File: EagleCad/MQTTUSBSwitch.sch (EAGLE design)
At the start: 41 parts, among them J1 10117835-002LF, J2 GSB4211311WEU, Q1 MMBT2222, Q2 MMBT2222, Q3 MMBT2222, Q4 MMBT2222, U1 MIC5504-3.3YM5_TR, X2 MICROBUILDER_RELAY_LATCHINGEE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, X3 MICROBUILDER_RELAY_LATCHINGEE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

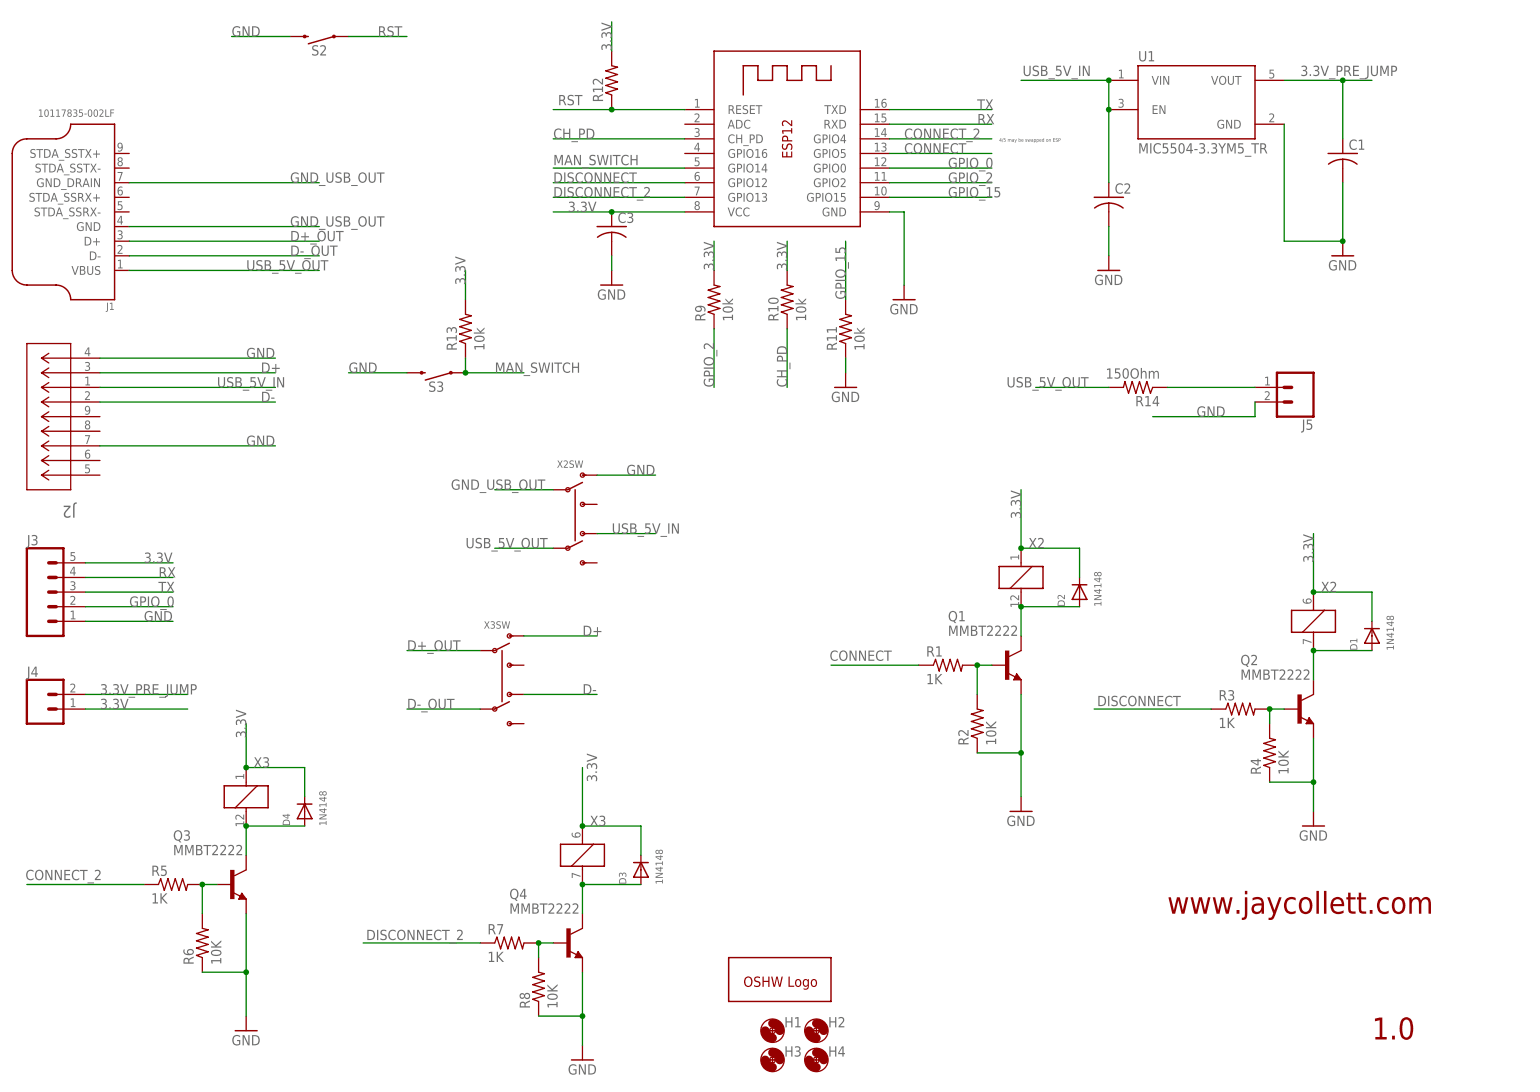
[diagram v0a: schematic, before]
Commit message: first pass at v2.1 which simplifies relay driving with a unla2803 and a port expander to only use 2 GPIO pins on ESP8266
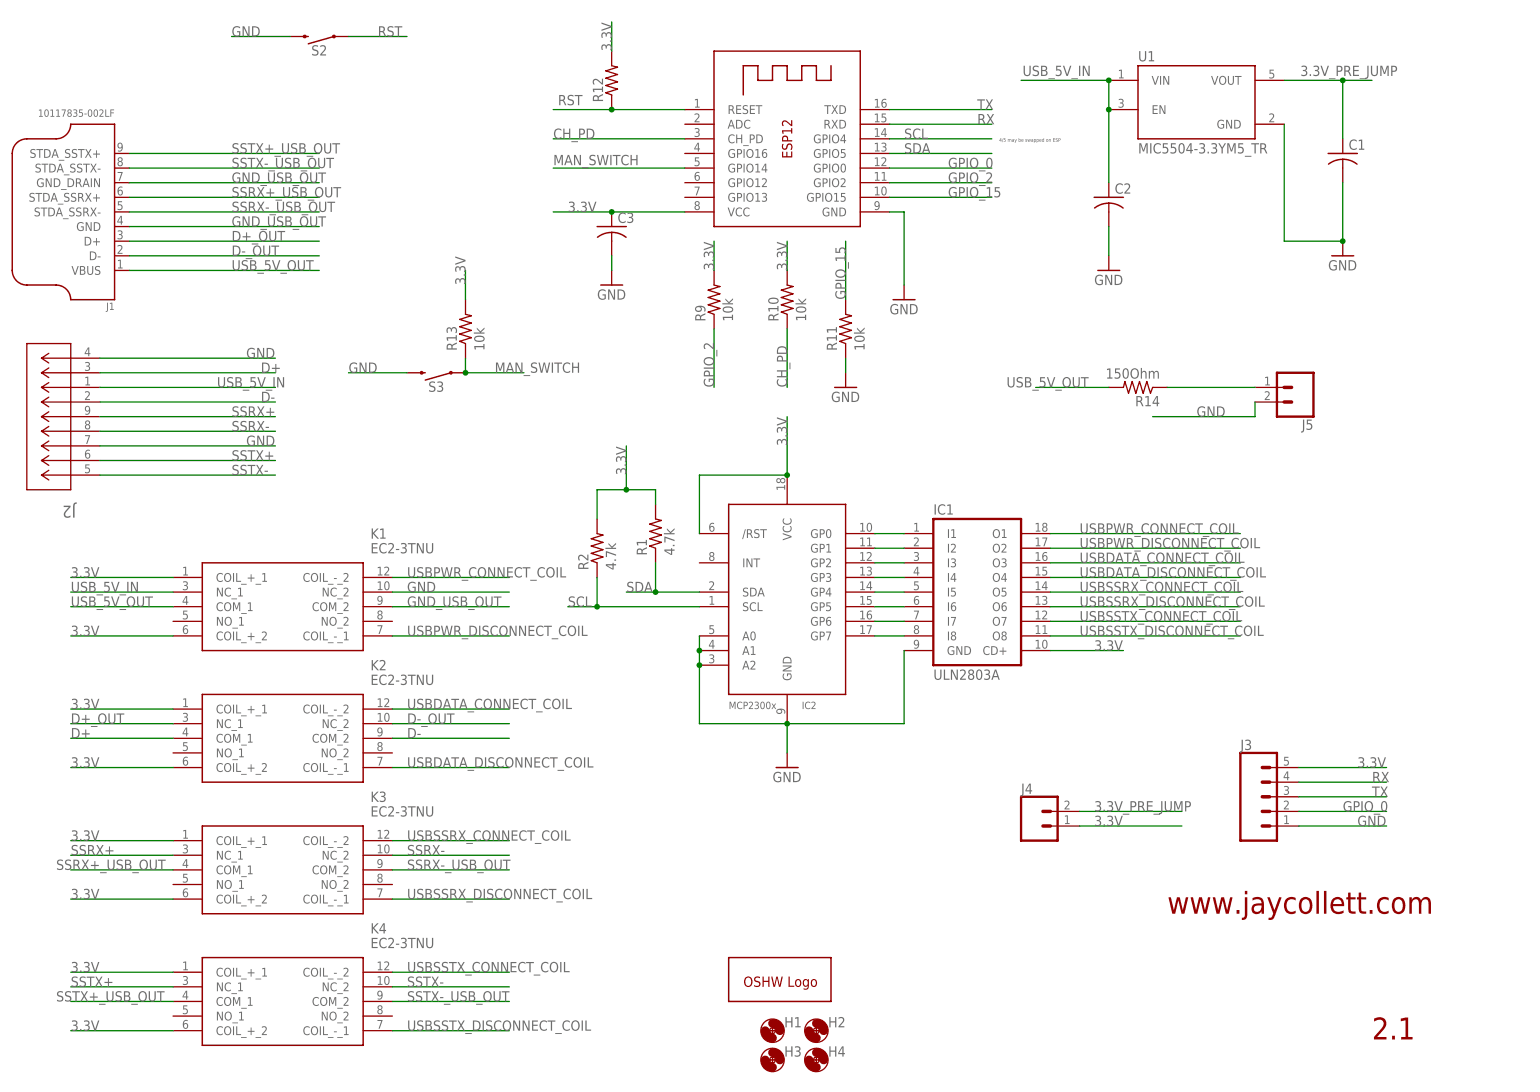
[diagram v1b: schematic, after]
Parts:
- removed D1, D2, D3, D4: 1N4148, adafruit:DIODESOD-323F
- removed Q1, Q2, Q3, Q4: MMBT2222, MMBT2222_:MMBT2222
- removed R3, R5, R7: 1K, adafruit:R-US_M0805
- removed R4, R6, R8: 10K, adafruit:R-US_M0805
- removed X2, X3: MICROBUILDER_RELAY_LATCHINGEE2NUH, AdaFruitLatchingRelay:MICROBUILDER_RELAY_LATCHINGEE2NUH
- added IC1: ULN2803A, uln-udn:ULN2804A
- added IC2: MCP23008/P, adafruit:MCP23008/P
- added K1, K2, K3, K4: EC2-3TNU, SamacSys_Parts:EC2-3TNU
- R1: value 1K -> 4.7k; device adafruit:R-US_M0805 -> adafruit:R-US_R0805
- R2: value 10K -> 4.7k; device adafruit:R-US_M0805 -> adafruit:R-US_R0805
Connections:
- removed net CONNECT: R1.1, X1.GPIO5
- removed net CONNECT_2: R5.1, X1.GPIO4
- removed net DISCONNECT: R3.1, X1.GPIO12
- removed net DISCONNECT_2: R7.1, X1.GPIO13
- removed net N$10: D2.A, Q1.C, X2SET.2
- removed net N$11: D1.A, Q2.C, X2RESET.2
- removed net N$12: Q1.B, R1.2, R2.2
- removed net N$13: Q2.B, R3.2, R4.2
- removed net N$14: D4.A, Q3.C, X3SET.2
- removed net N$15: D3.A, Q4.C, X3RESET.2
- removed net N$16: Q3.B, R5.2, R6.2
- removed net N$17: Q4.B, R7.2, R8.2
- new net N$2: IC1.I1, IC2.GP0
- new net N$3: IC1.I2, IC2.GP1
- new net N$4: IC1.I3, IC2.GP2
- new net N$5: IC1.I4, IC2.GP3
- new net N$6: IC1.I5, IC2.GP4
- new net N$7: IC1.I6, IC2.GP5
- new net N$8: IC1.I7, IC2.GP6
- new net N$9: IC1.I8, IC2.GP7
- new net SCL: IC2.SCL, R2.1, X1.GPIO4
- new net SDA: IC2.SDA, R1.1, X1.GPIO5
- new net SSRX+: J2.9, K3.NC_1
- new net SSRX+_USB_OUT: J1.STDA_SSRX+, K3.COM_1
- new net SSRX-: J2.8, K3.NC_2
- new net SSRX-_USB_OUT: J1.STDA_SSRX-, K3.COM_2
- new net SSTX+: J2.6, K4.NC_1
- new net SSTX+_USB_OUT: J1.STDA_SSTX+, K4.COM_1
- new net SSTX-: J2.5, K4.NC_2
- new net SSTX-_USB_OUT: J1.STDA_SSTX-, K4.COM_2
- new net USBDATA_CONNECT_COIL: IC1.O3, K2.COIL_-_2
- new net USBDATA_DISCONNECT_COIL: IC1.O4, K2.COIL_-_1
- new net USBPWR_CONNECT_COIL: IC1.O1, K1.COIL_-_2
- new net USBPWR_DISCONNECT_COIL: IC1.O2, K1.COIL_-_1
- new net USBSSRX_CONNECT_COIL: IC1.O5, K3.COIL_-_2
- new net USBSSRX_DISCONNECT_COIL: IC1.O6, K3.COIL_-_1
- new net USBSSTX_CONNECT_COIL: IC1.O7, K4.COIL_-_2
- new net USBSSTX_DISCONNECT_COIL: IC1.O8, K4.COIL_-_1
- net 3.3V: now also IC1.CD+, IC2./RST, IC2.VCC, K1.COIL_+_1, K1.COIL_+_2, K2.COIL_+_1, K2.COIL_+_2, K3.COIL_+_1, K3.COIL_+_2, K4.COIL_+_1, K4.COIL_+_2, R1.2, R2.2; no longer D1.C, D2.C, D3.C, D4.C, X2RESET.1, X2SET.1, X3RESET.1, X3SET.1
- net D+: now also K2.COM_1; no longer X3SW.O1
- net D+_OUT: now also K2.NC_1; no longer X3SW.P1
- net D-: now also K2.COM_2; no longer X3SW.O2
- net D-_OUT: now also K2.NC_2; no longer X3SW.P2
- net GND: now also IC1.GND, IC2.A0, IC2.A1, IC2.A2, IC2.GND, K1.NC_2; no longer Q1.E, Q2.E, Q3.E, Q4.E, R2.1, R4.1, R6.1, R8.1, X2SW.O1
- net GND_USB_OUT: now also K1.COM_2; no longer X2SW.P1
- net USB_5V_IN: now also K1.NC_1; no longer X2SW.O2
- net USB_5V_OUT: now also K1.COM_1; no longer X2SW.P2
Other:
- note added: "2.1"
- note removed: "1.0"
- moved on the sheet: J3, J4, R1, R2

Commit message: New layout and routing for v2.1
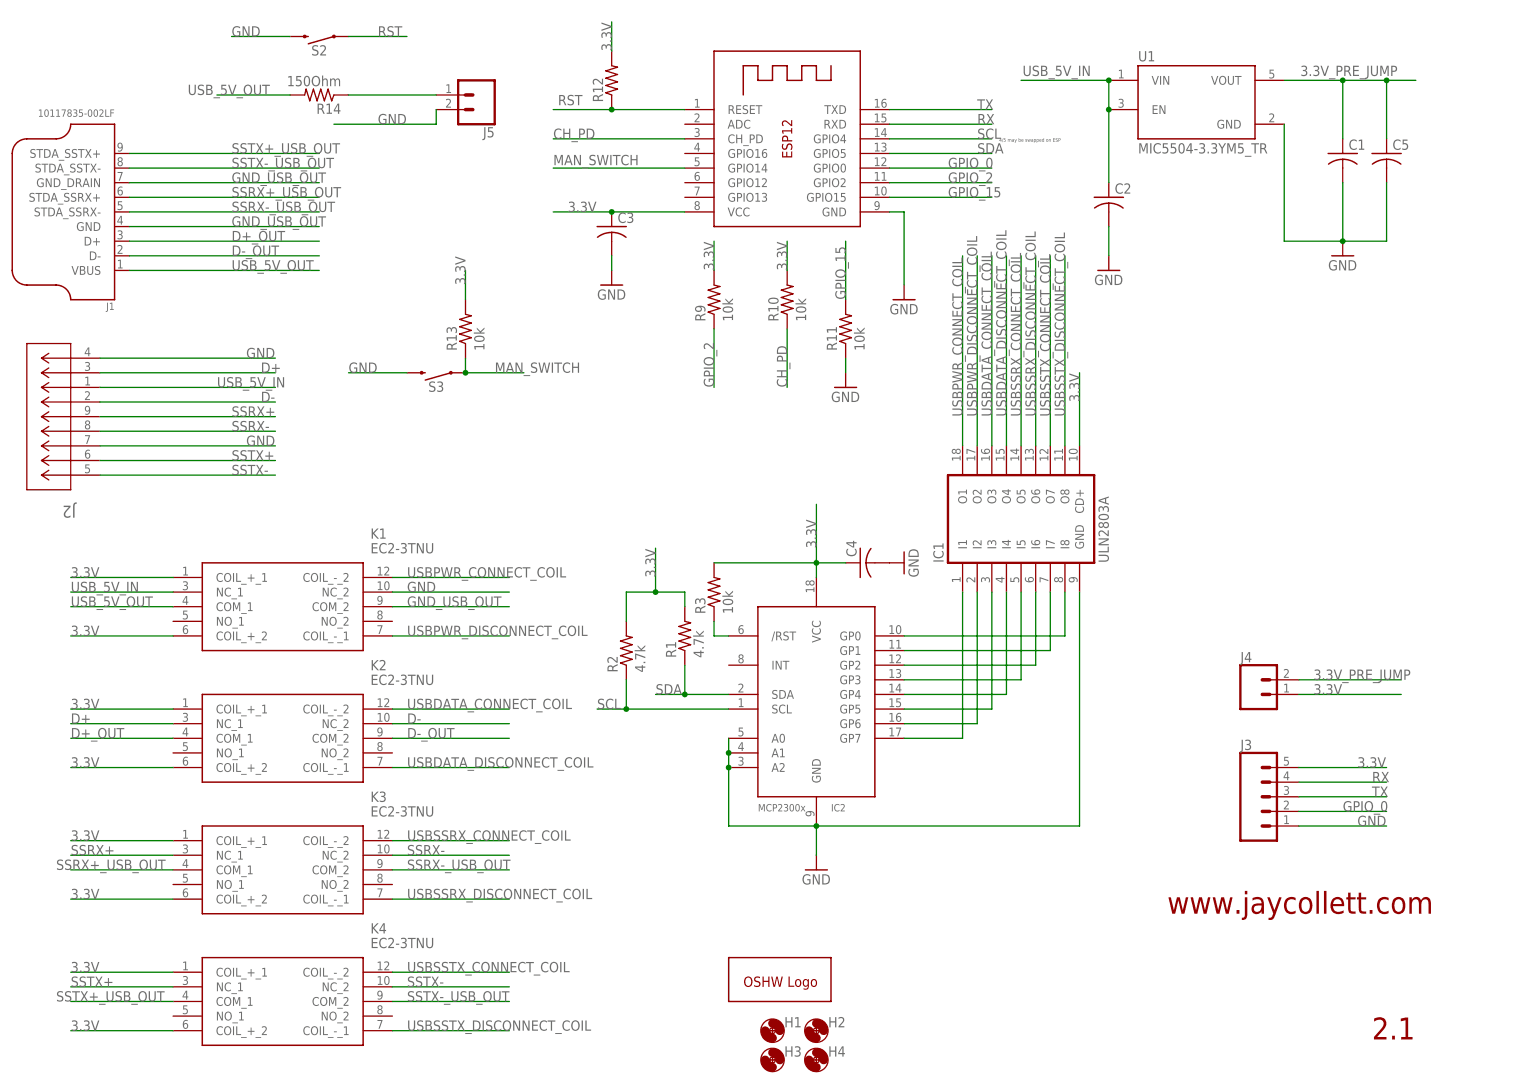
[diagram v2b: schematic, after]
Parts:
- added C4, C5: (no value), adafruit:C-USC0805
- added R3: 10k, adafruit:R-US_R0805
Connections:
- new net N$10: IC2./RST, R3.1
- net 3.3V: now also C4.1, R3.2; no longer IC2./RST
- net 3.3V_PRE_JUMP: now also C5.1
- net D+: now also K2.NC_1; no longer K2.COM_1
- net D+_OUT: now also K2.COM_1; no longer K2.NC_1
- net D-: now also K2.NC_2; no longer K2.COM_2
- net D-_OUT: now also K2.COM_2; no longer K2.NC_2
- net GND: now also C4.2, C5.2
- net N$2: now also IC1.I8; no longer IC1.I1
- net N$3: now also IC1.I7; no longer IC1.I2
- net N$4: now also IC1.I6; no longer IC1.I3
- net N$5: now also IC1.I5; no longer IC1.I4
- net N$6: now also IC1.I4; no longer IC1.I5
- net N$7: now also IC1.I3; no longer IC1.I6
- net N$8: now also IC1.I2; no longer IC1.I7
- net N$9: now also IC1.I1; no longer IC1.I8
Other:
- moved on the sheet: IC1, IC2, J4, J5, R1, R14, R2
